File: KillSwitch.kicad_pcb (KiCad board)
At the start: 2 copper layers, 40.5 x 44.2 mm, 25 parts, among them J0 Screw_Terminal_1x04, J1 CONN_01X04, J2 CONN_01X04, J3 CONN_01X02, J4 CONN_01X04, Q0 IRF1324PBF, Q1 IRF1324PBF, Q2 IRF1324PBF, Q3 IRF1324PBF, U0 NC7SZ08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

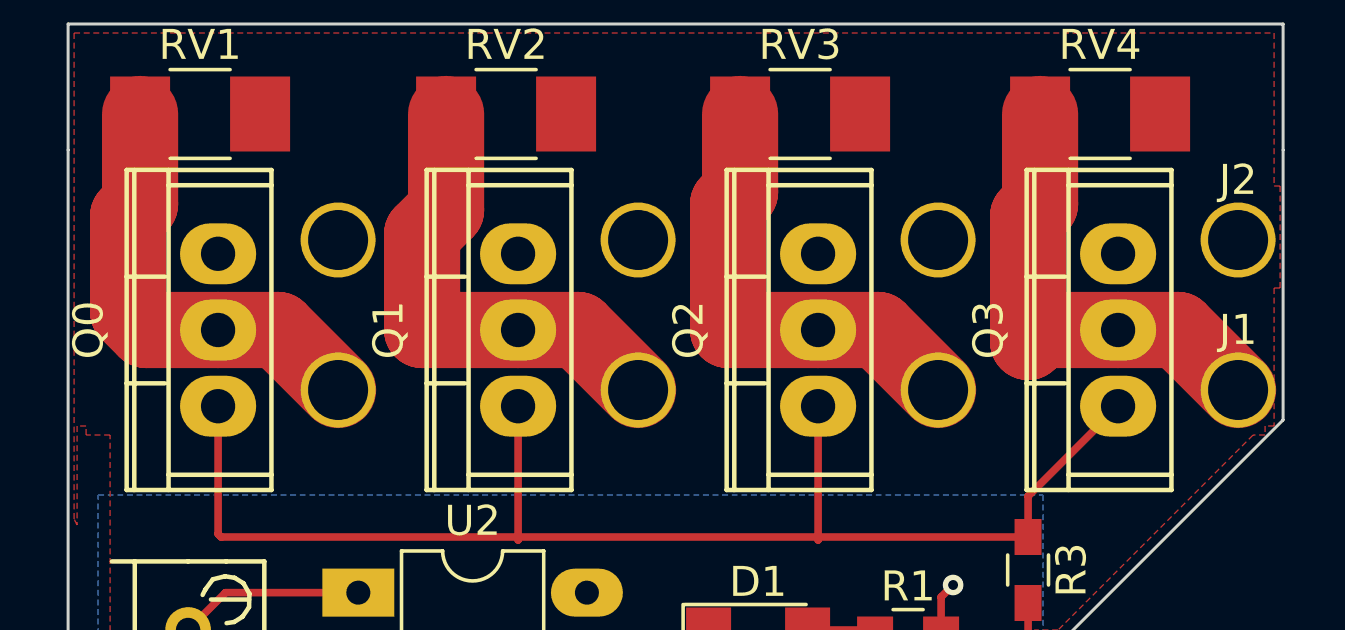
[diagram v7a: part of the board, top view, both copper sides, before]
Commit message: Add traces on bottom plane as well as top for high current
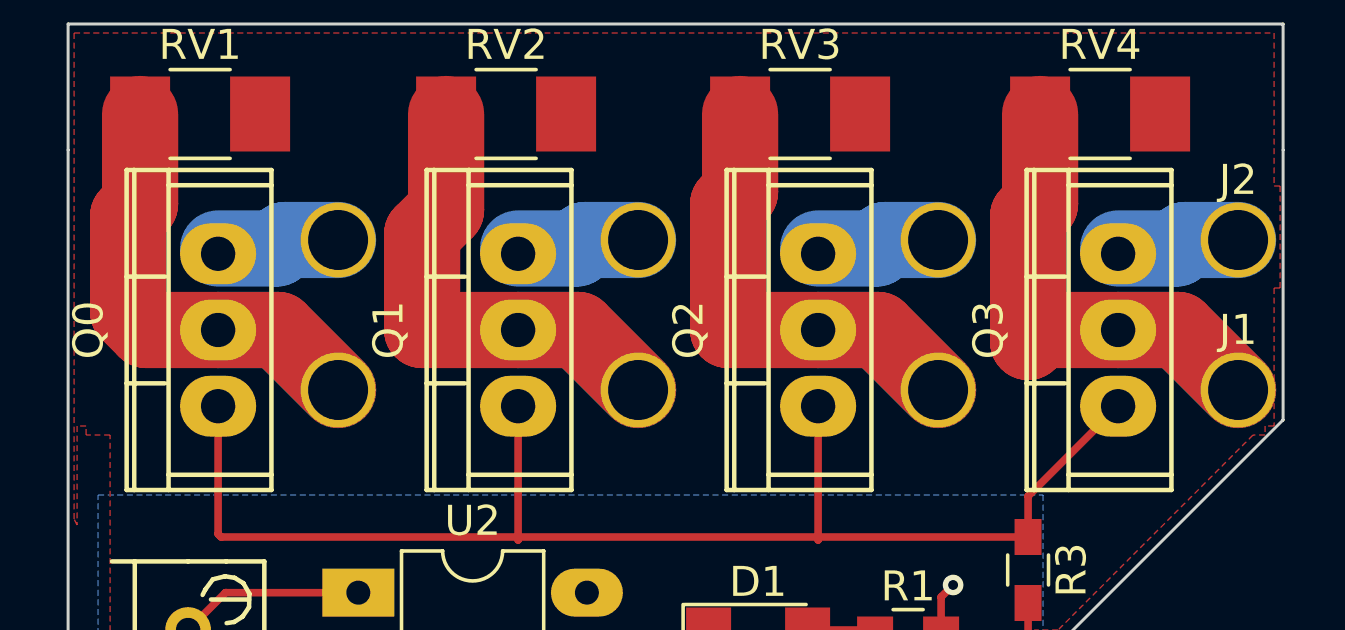
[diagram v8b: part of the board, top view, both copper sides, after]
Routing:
- net Earth: track 0.00 -> 16.5 mm
- net Net-(J2-Pad3): track 15.6 -> 20.4 mm
- net Net-(J2-Pad4): track 14.8 -> 19.7 mm
- net Net-(J2-Pad2): track 15.2 -> 20.0 mm
- net Net-(J2-Pad1): track 15.8 -> 20.6 mm
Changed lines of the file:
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@@
-(kicad_pcb (version 4) (host pcbnew 4.0.6)
+(kicad_pcb (version 20170123) (host pcbnew no-vcs-found-ea855c1~58~ubuntu16.04.1)
   (general
     (links 59)
     (no_connects 0)
-    (area 175.949999 56.949999 216.550001 97.050001)
+    (area 160.02 49.5647 223.086134 156.335001)
     (thickness 0.8128)
     (drawings 12)
-    (tracks 92)
+    (tracks 112)
     (zones 0)
     (modules 25)
@@
   )
   (setup
-    (last_trace_width 0.254)
+    (last_trace_width 2.54)
+    (user_trace_width 2.54)
     (trace_clearance 0.1524)
     (zone_clearance 0.1524)
@@
       (hpglpenspeed 20)
       (hpglpendiameter 15)
-      (hpglpenoverlay 2)
       (psnegative false)
       (psa4output false)
@@
   (segment (start 196.95 85.05) (end 197 85) (width 0.254) (layer Top) (net 1))
   (segment (start 193.539 72) (end 193.294 71.755) (width 0.254) (layer Top) (net 1))
+  (segment (start 185 60) (end 183.232234 60) (width 2.54) (layer Bottom) (net 2))
+  (segment (start 183.232234 60) (end 182.950044 60.28219) (width 2.54) (layer Bottom) (net 2))
+  (segment (start 182.950044 60.28219) (end 181 60.28219) (width 2.54) (layer Bottom) (net 2))
+  (segment (start 195 60) (end 193.232234 60) (width 2.54) (layer Bottom) (net 2))
+  (segment (start 193.232234 60) (end 192.950044 60.28219) (width 2.54) (layer Bottom) (net 2))
+  (segment (start 192.950044 60.28219) (end 191 60.28219) (width 2.54) (layer Bottom) (net 2))
+  (segment (start 205 60) (end 203.232234 60) (width 2.54) (layer Bottom) (net 2))
+  (segment (start 202.950044 60.28219) (end 201 60.28219) (width 2.54) (layer Bottom) (net 2))
+  (segment (start 203.232234 60) (end 202.950044 60.28219) (width 2.54) (layer Bottom) (net 2))
+  (segment (start 215 60) (end 213.232234 60) (width 2.54) (layer Bottom) (net 2))
+  (segment (start 212.950044 60.28219) (end 211 60.28219) (width 2.54) (layer Bottom) (net 2))
+  (segment (start 213.232234 60) (end 212.950044 60.28219) (width 2.54) (layer Bottom) (net 2))
   (segment (start 180 78.08) (end 180 85.95) (width 0.254) (layer Top) (net 3))
   (segment (start 180 85.95) (end 180.05 86) (width 0.254) (layer Top) (net 3))
@@
   (segment (start 205.295 74.295) (end 207 76) (width 0.254) (layer Top) (net 13))
   (segment (start 201 87) (end 201.05 86.35) (width 0.254) (layer Top) (net 13))
+  (segment (start 215 65) (end 213 63) (width 2.54) (layer Bottom) (net 14))
+  (segment (start 213 63) (end 211 63) (width 2.54) (layer Bottom) (net 14))
   (segment (start 208.4 55.8) (end 208.4 58.8) (width 2.54) (layer Top) (net 14))
   (segment (start 208.4 63) (end 211 63) (width 2.54) (layer Top) (net 14))
@@
   (segment (start 211 63) (end 213 63) (width 2.54) (layer Top) (net 14))
   (segment (start 213 63) (end 215 65) (width 2.54) (layer Top) (net 14))
+  (segment (start 205 65) (end 203 63) (width 2.54) (layer Bottom) (net 15))
+  (segment (start 203 63) (end 201 63) (width 2.54) (layer Bottom) (net 15))
   (segment (start 198.4 55.8) (end 198.4 58.4) (width 2.54) (layer Top) (net 15))
   (segment (start 198 63) (end 201 63) (width 2.54) (layer Top) (net 15))
@@
   (segment (start 201 63) (end 203 63) (width 2.54) (layer Top) (net 15))
   (segment (start 203 63) (end 205 65) (width 2.54) (layer Top) (net 15))
+  (segment (start 195 65) (end 193 63) (width 2.54) (layer Bottom) (net 16))
+  (segment (start 193 63) (end 191 63) (width 2.54) (layer Bottom) (net 16))
   (segment (start 188.6 55.8) (end 188.6 59) (width 2.54) (layer Top) (net 16))
   (segment (start 187.8 63) (end 191 63) (width 2.54) (layer Top) (net 16))
@@
   (segment (start 191 63) (end 193 63) (width 2.54) (layer Top) (net 16))
   (segment (start 193 63) (end 195 65) (width 2.54) (layer Top) (net 16))
+  (segment (start 185 65) (end 183 63) (width 2.54) (layer Bottom) (net 17))
+  (segment (start 183 63) (end 181 63) (width 2.54) (layer Bottom) (net 17))
   (segment (start 178.4 55.8) (end 178.4 58.8) (width 2.54) (layer Top) (net 17))
   (segment (start 178.6 63) (end 181 63) (width 2.54) (layer Top) (net 17))
